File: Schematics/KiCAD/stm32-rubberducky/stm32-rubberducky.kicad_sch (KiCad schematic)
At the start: 1 part, among them U1 STM32F103C6T6

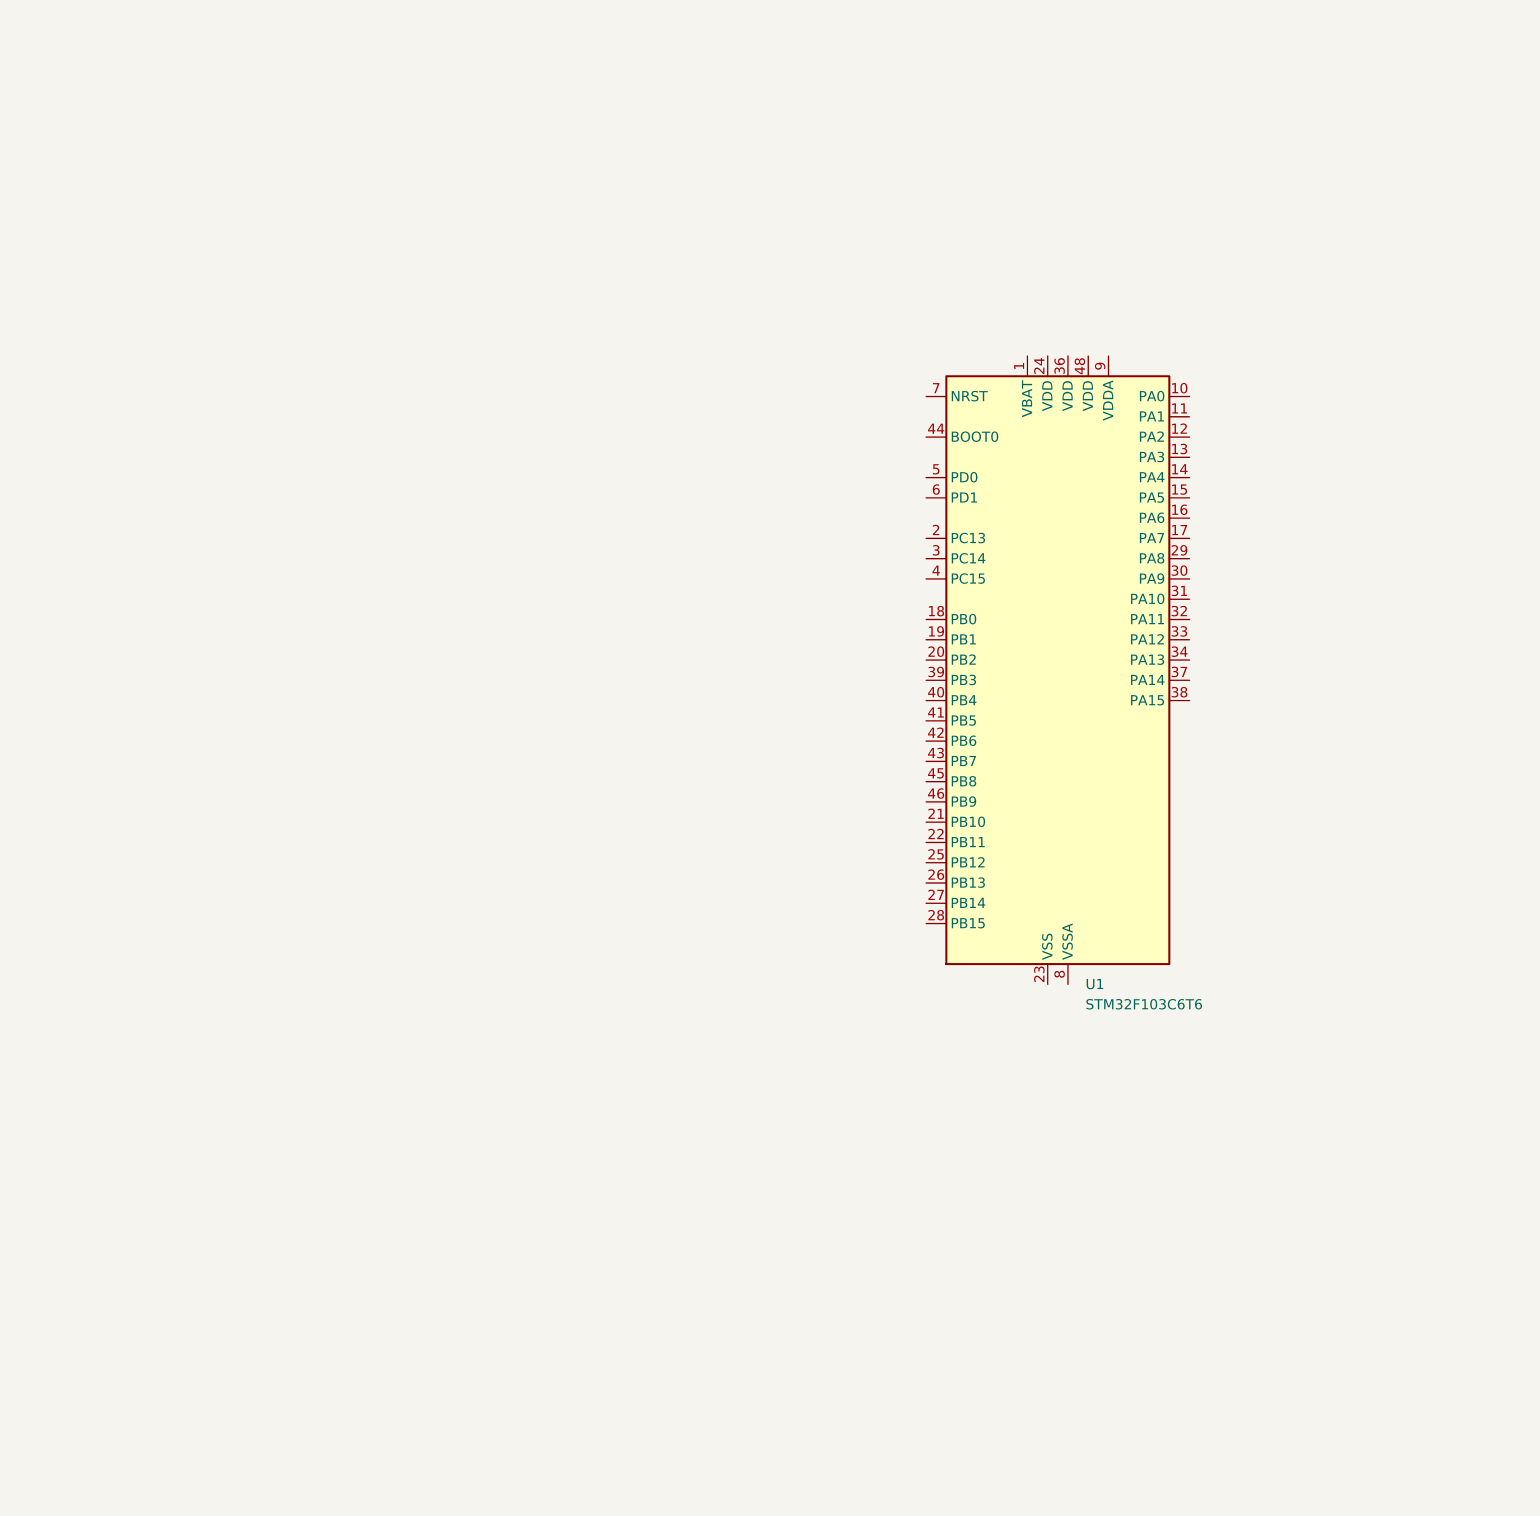
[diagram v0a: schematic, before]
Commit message: added STM32 basic components to the schematic. Now only the SD card interface & the USB interface is missing
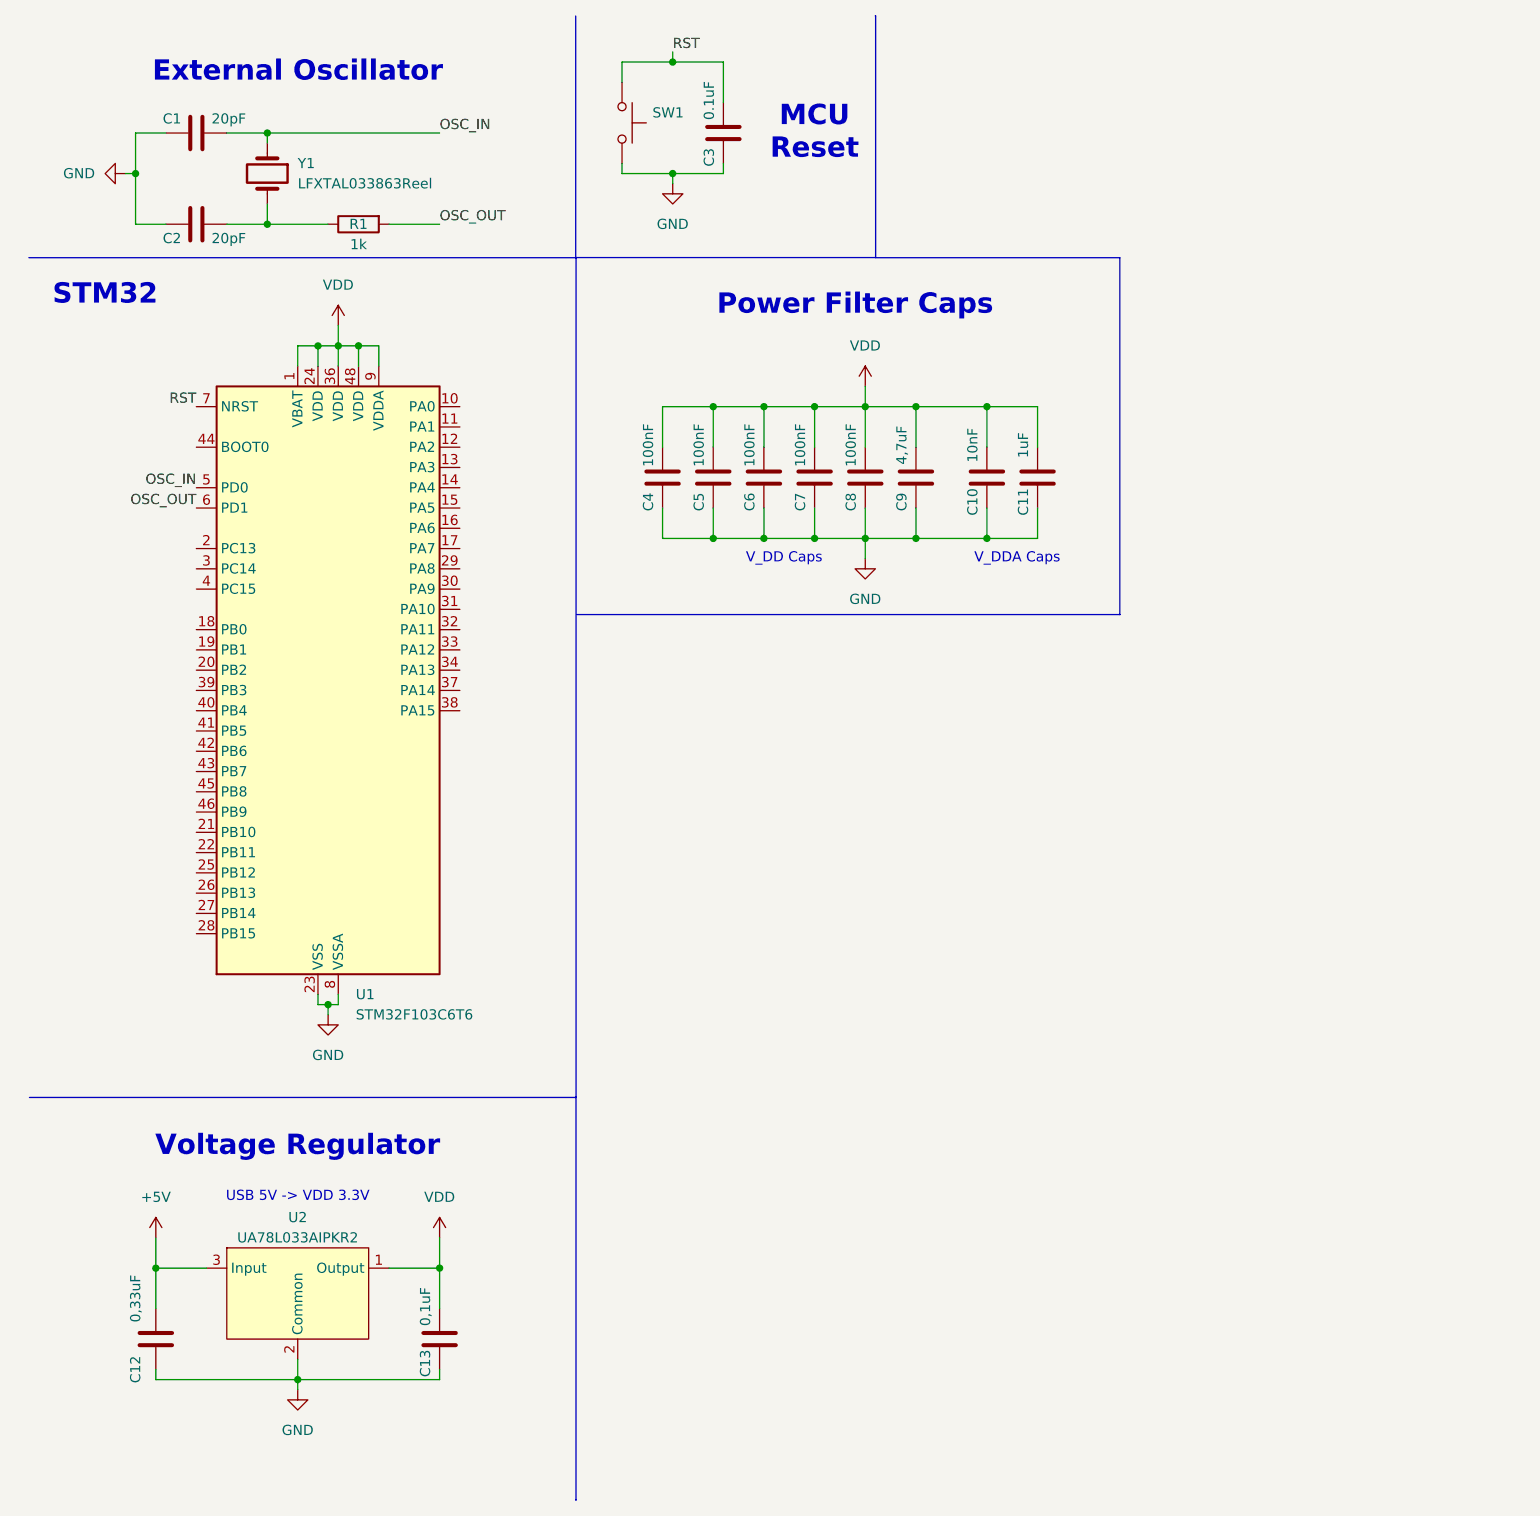
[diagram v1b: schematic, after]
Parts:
- added C1, C2: 20pF, symbol Device:C
- added C10: 10nF, symbol Device:C
- added C11: 1uF, symbol Device:C
- added C12: 0,33uF, symbol Device:C
- added C13: 0,1uF, symbol Device:C
- added C3: 0.1uF, symbol Device:C
- added C4, C5, C6, C7, C8: 100nF, symbol Device:C
- added C9: 4,7uF, symbol Device:C
- added R1: 1k, symbol Device:R
- added SW1: ~, symbol Switch:SW_Push
- added U2: UA78L033AIPKR2, Package_TO_SOT_SMD:SOT-89-3_Handsoldering, symbol project_lib:UA78L033AIPKR2
- added Y1: LFXTAL033863Reel, symbol Device:Crystal
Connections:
- net VDD: now reaches U1.1 (VBAT)
- net VDD: now also U1.24 (VDD), U1.36 (VDD), U1.48 (VDD), U1.9 (VDDA), C10.2, C11.2, C13.2, C4.2, C5.2, C6.2, C7.2, C8.2, C9.2, U2.1 (Output)
- net GND: now reaches U1.23 (VSS), U1.35 (VSS), U1.47 (VSS)
- net GND: now also U1.8 (VSSA), C1.1, C10.1, C11.1, C12.1, C13.1, C2.1, C3.1, C4.1, C5.1, C6.1, C7.1, C8.1, C9.1, SW1.2, U2.2 (Common)
- net OSC_IN: now reaches U1.5 (PD0)
- net OSC_IN: now also C1.2, Y1.1
- net OSC_OUT: now reaches U1.6 (PD1)
- net OSC_OUT: now also R1.2
- net RST: now reaches U1.7 (NRST)
- net RST: now also C3.2, SW1.1
- new net: C2.2, R1.1, Y1.2
- new net +5V: C12.2, U2.3 (Input)
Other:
- note added: "External Oscillator"
- note added: "MCU Reset"
- note added: "Power Filter Caps"
- note added: "STM32"
- note added: "USB 5V -> VDD 3.3V"
- note added: "V_DD Caps"
- note added: "V_DDA Caps"
- note added: "Voltage Regulator"
- moved on the sheet: U1

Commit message: added pinouts of peripherals to doc and allmost finished the schematic
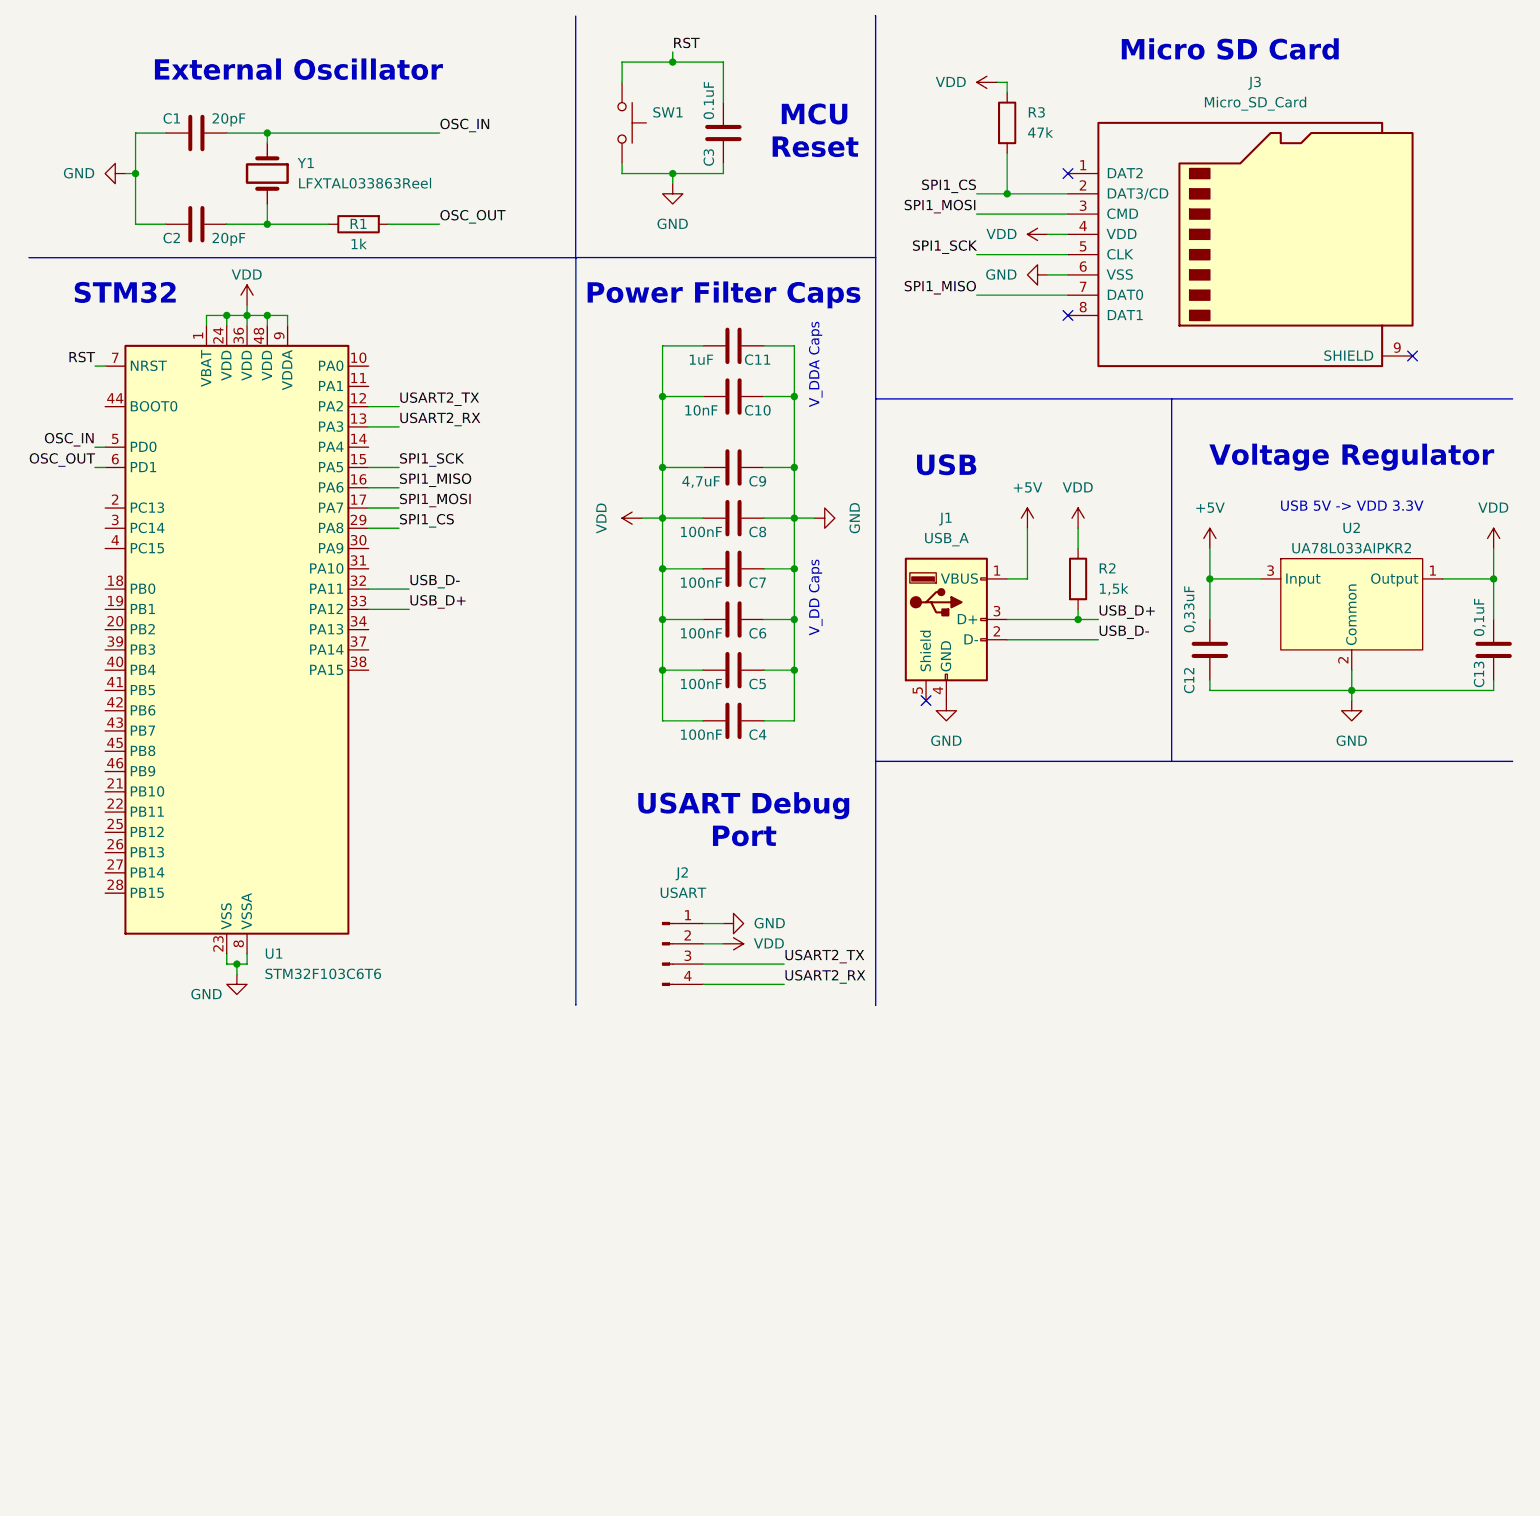
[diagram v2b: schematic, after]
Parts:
- added J1: USB_A, symbol Connector:USB_A
- added J2: USART, symbol Connector:Conn_01x04_Pin
- added J3: Micro_SD_Card, symbol Connector:Micro_SD_Card
- added R2: 1,5k, symbol Device:R
- added R3: 47k, symbol Device:R
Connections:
- net +5V: now also J1.1 (VBUS)
- net GND: now also J1.4 (GND), J2.1 (Pin_1), J3.6 (VSS)
- net VDD: now also J2.2 (Pin_2), J3.4 (VDD), R2.1, R3.1
- net USART2_TX: now reaches U1.12 (PA2)
- net USART2_TX: now also J2.3 (Pin_3)
- net USART2_RX: now reaches U1.13 (PA3)
- net USART2_RX: now also J2.4 (Pin_4)
- net SPI1_SCK: now reaches U1.15 (PA5)
- net SPI1_SCK: now also J3.5 (CLK)
- net SPI1_MISO: now reaches U1.16 (PA6)
- net SPI1_MISO: now also J3.7 (DAT0)
- net SPI1_MOSI: now reaches U1.17 (PA7)
- net SPI1_MOSI: now also J3.3 (CMD)
- net SPI1_CS: now reaches U1.29 (PA8)
- net SPI1_CS: now also J3.2 (DAT3/CD), R3.2
- net USB_D-: now reaches U1.32 (PA11)
- net USB_D-: now also J1.2 (D-)
- net USB_D+: now reaches U1.33 (PA12)
- net USB_D+: now also J1.3 (D+), R2.2
- no-connect marks 0 -> 4
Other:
- note added: "Micro SD Card"
- note added: "USART Debug Port"
- note added: "USB"
- moved on the sheet: C10, C11, C12, C13, C4, C5, C6, C7, C8, C9, U1, U2
